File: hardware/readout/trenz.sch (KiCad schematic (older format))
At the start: 1 part, among them J2 Trenz_Module

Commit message: working
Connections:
- net MGT_RX_P3: now reaches J2.A1 (MGT_RX3_P)
- net MGT_TX_N3: now reaches J2.A10 (MGT_TX3_N)
- net MGT_RX_P1: now reaches J2.A13 (MGT_RX1_P)
- net MGT_TX_P2: now reaches J2.A14 (MGT_TX2_P)
- net MGT_RX_N1: now reaches J2.A15 (MGT_RX1_N)
- net MGT_TX_N2: now reaches J2.A16 (MGT_TX2_N)
- net MGT_TX_P1: now reaches J2.A20 (MGT_TX1_P)
- net MGT_TX_N1: now reaches J2.A22 (MGT_TX1_N)
- net MGT_RX_N3: now reaches J2.A3 (MGT_RX3_N)
- net TRIG8: now reaches J2.A49 (B34_L10_P)
- net TRIG9: now reaches J2.A51 (B34_L10_N)
- net TRIG10: now reaches J2.A53 (B34_L11_N)
- net TRIG11: now reaches J2.A55 (B34_L11_P)
- net TRIG12: now reaches J2.A57 (B34_L12_N)
- net TRIG13: now reaches J2.A59 (B34_L12_P)
- net TRIG14: now reaches J2.A63 (B34_L17_N)
- net TRIG15: now reaches J2.A65 (B34_L17_P)
- net TRIG16: now reaches J2.A67 (B34_L21_P)
- net TRIG17: now reaches J2.A69 (B34_L21_N)
- net MGT_RX_P2: now reaches J2.A7 (MGT_RX2_P)
- net TRIG18: now reaches J2.A71 (B34_L19_N)
- net TRIG19: now reaches J2.A73 (B34_L19_P)
- net TRIG20: now reaches J2.A75 (B34_L22_N)
- net TRIG21: now reaches J2.A77 (B34_L22_P)
- net TRIG22: now reaches J2.A79 (B34_L23_N)
- net MGT_TX_P3: now reaches J2.A8 (MGT_TX3_P)
- net TRIG23: now reaches J2.A81 (B34_L23_P)
- net MGT_RX_N2: now reaches J2.A9 (MGT_RX2_N)
- net DATA_RX_N renamed MGT_RX_N0
- net DATA_RX_P renamed MGT_RX_P0
- net DATA_TX_N renamed MGT_TX_N0
- net DATA_TX_P renamed MGT_TX_P0
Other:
- moved on the sheet: J2A, J2B

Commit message: working on schematic
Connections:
- net TRIG0: now also J2.A85 (B14_L24_N); no longer J2.A31 (B34_L2_P)
- net TRIG1: now also J2.A87 (B14_L24_P); no longer J2.A33 (B34_L2_N)
- net TRIG10: now also J2.B63 (B14_L15_P); no longer J2.A53 (B34_L11_N)
- net TRIG11: now also J2.B65 (B14_L15_N); no longer J2.A55 (B34_L11_P)
- net TRIG12: now also J2.B75 (B14_L10_P); no longer J2.A57 (B34_L12_N)
- net TRIG13: now also J2.B77 (B14_L10_N); no longer J2.A59 (B34_L12_P)
- net TRIG14: now also J2.B79 (B14_L16_P); no longer J2.A63 (B34_L17_N)
- net TRIG15: now also J2.B81 (B14_L16_N); no longer J2.A65 (B34_L17_P)
- net TRIG16: now also J2.B85 (B14_L18_N); no longer J2.A67 (B34_L21_P)
- net TRIG17: now also J2.B87 (B14_L18_P); no longer J2.A69 (B34_L21_N)
- net TRIG18: now also J2.B89 (B14_L17_N); no longer J2.A71 (B34_L19_N)
- net TRIG19: now also J2.B91 (B14_L17_P); no longer J2.A73 (B34_L19_P)
- net TRIG2: now also J2.A89 (B14_L23_N); no longer J2.A35 (B34_L1_P)
- net TRIG20: now also J2.B93 (B14_L20_P); no longer J2.A75 (B34_L22_N)
- net TRIG21: now also J2.B95 (B14_L20_N); no longer J2.A77 (B34_L22_P)
- net TRIG22: now also J2.B97 (B14_L25); no longer J2.A79 (B34_L23_N)
- net TRIG23: now also J2.B99 (B14_L0); no longer J2.A81 (B34_L23_P)
- net TRIG3: now also J2.A91 (B14_L23_P); no longer J2.A37 (B34_L1_N)
- net TRIG4: now also J2.A93 (B14_L21_P); no longer J2.A39 (B34_L4_P)
- net TRIG5: now also J2.A95 (B14_L21_N); no longer J2.A41 (B34_L4_N)
- net TRIG6: now also J2.B55 (B14_L4_P); no longer J2.A43 (B34_L5_P)
- net TRIG7: now also J2.B57 (B14_L4_N); no longer J2.A45 (B34_L5_N)
- net TRIG8: now also J2.B59 (B14_L7_N); no longer J2.A49 (B34_L10_P)
- net TRIG9: now also J2.B61 (B14_L7_P); no longer J2.A51 (B34_L10_N)
- net TRIG24: now reaches J2.B56 (B14_L5_P)
- net TRIG25: now reaches J2.B58 (B14_L5_N)
- net TRIG26: now reaches J2.B60 (B14_L8_P)
- net TRIG27: now reaches J2.B62 (B14_L8_N)
- net TRIG28: now reaches J2.B64 (B14_L9_P)
- net TRIG29: now reaches J2.B66 (B14_L9_N)
- net TRIG30: now reaches J2.B74 (B14_L11_N)
- net TRIG31: now reaches J2.B76 (B14_L11_P)
- net TRIG32: now reaches J2.B78 (B14_L14_N)
- net TRIG33: now reaches J2.B80 (B14_L14_P)
- net TRIG34: now reaches J2.B82 (B14_L12_P)
- net TRIG35: now reaches J2.B84 (B14_L12_N)
- net TRIG36: now reaches J2.B86 (B14_L13_N)
- net TRIG37: now reaches J2.B88 (B14_L13_P)
- net TRIG38: now reaches J2.B92 (B14_L19_P)
- net TRIG39: now reaches J2.B94 (B14_L19_N)
- net TRIG40: now reaches J2.B96 (B14_L22_N)
- net TRIG41: now reaches J2.B98 (B14_L22_P)
- net TRIG66: now reaches J2.A32 (B34_L6_P)
- net TRIG67: now reaches J2.A34 (B34_L6_N)
- net TRIG68: now reaches J2.A36 (B34_L7_P)
- net TRIG69: now reaches J2.A38 (B34_L7_N)
- net TRIG70: now reaches J2.A40 (B34_L3_P)
- net TRIG71: now reaches J2.A42 (B34_L3_N)
- net TRIG72: now reaches J2.A44 (B34_L9_P)
- net TRIG73: now reaches J2.A46 (B34_L9_N)
- net TRIG74: now reaches J2.A50 (B34_L8_P)
- net TRIG75: now reaches J2.A52 (B34_L8_N)
- net TRIG76: now reaches J2.A54 (B34_L13_P)
- net TRIG77: now reaches J2.A56 (B34_L13_N)
- net TRIG78: now reaches J2.A58 (B34_L14_P)
- net TRIG79: now reaches J2.A60 (B34_L14_N)
- net TRIG80: now reaches J2.A62 (B34_L15_N)
- net TRIG81: now reaches J2.A64 (B34_L15_P)
- net TRIG82: now reaches J2.A68 (B34_L16_N)
- net TRIG83: now reaches J2.A70 (B34_L16_P)
- net TRIG84: now reaches J2.A72 (B34_L18_P)
- net TRIG85: now reaches J2.A74 (B34_L18_N)
- net TRIG86: now reaches J2.A76 (B34_L20_N)
- net TRIG87: now reaches J2.A78 (B34_L20_P)
- net TRIG88: now reaches J2.A80 (B34_L24_N)
- net TRIG89: now reaches J2.A82 (B34_L24_P)
- new net TRIG42: J2.A31 (B34_L2_P)
- new net TRIG43: J2.A33 (B34_L2_N)
- new net TRIG44: J2.A35 (B34_L1_P)
- new net TRIG45: J2.A37 (B34_L1_N)
- new net TRIG46: J2.A39 (B34_L4_P)
- new net TRIG47: J2.A41 (B34_L4_N)
- new net TRIG48: J2.A43 (B34_L5_P)
- new net TRIG49: J2.A45 (B34_L5_N)
- new net TRIG50: J2.A49 (B34_L10_P)
- new net TRIG51: J2.A51 (B34_L10_N)
- new net TRIG52: J2.A53 (B34_L11_N)
- new net TRIG53: J2.A55 (B34_L11_P)
- new net TRIG54: J2.A57 (B34_L12_N)
- new net TRIG55: J2.A59 (B34_L12_P)
- new net TRIG56: J2.A63 (B34_L17_N)
- new net TRIG57: J2.A65 (B34_L17_P)
- new net TRIG58: J2.A67 (B34_L21_P)
- new net TRIG59: J2.A69 (B34_L21_N)
- new net TRIG60: J2.A71 (B34_L19_N)
- new net TRIG61: J2.A73 (B34_L19_P)
- new net TRIG62: J2.A75 (B34_L22_N)
- new net TRIG63: J2.A77 (B34_L22_P)
- new net TRIG64: J2.A79 (B34_L23_N)
- new net TRIG65: J2.A81 (B34_L23_P)

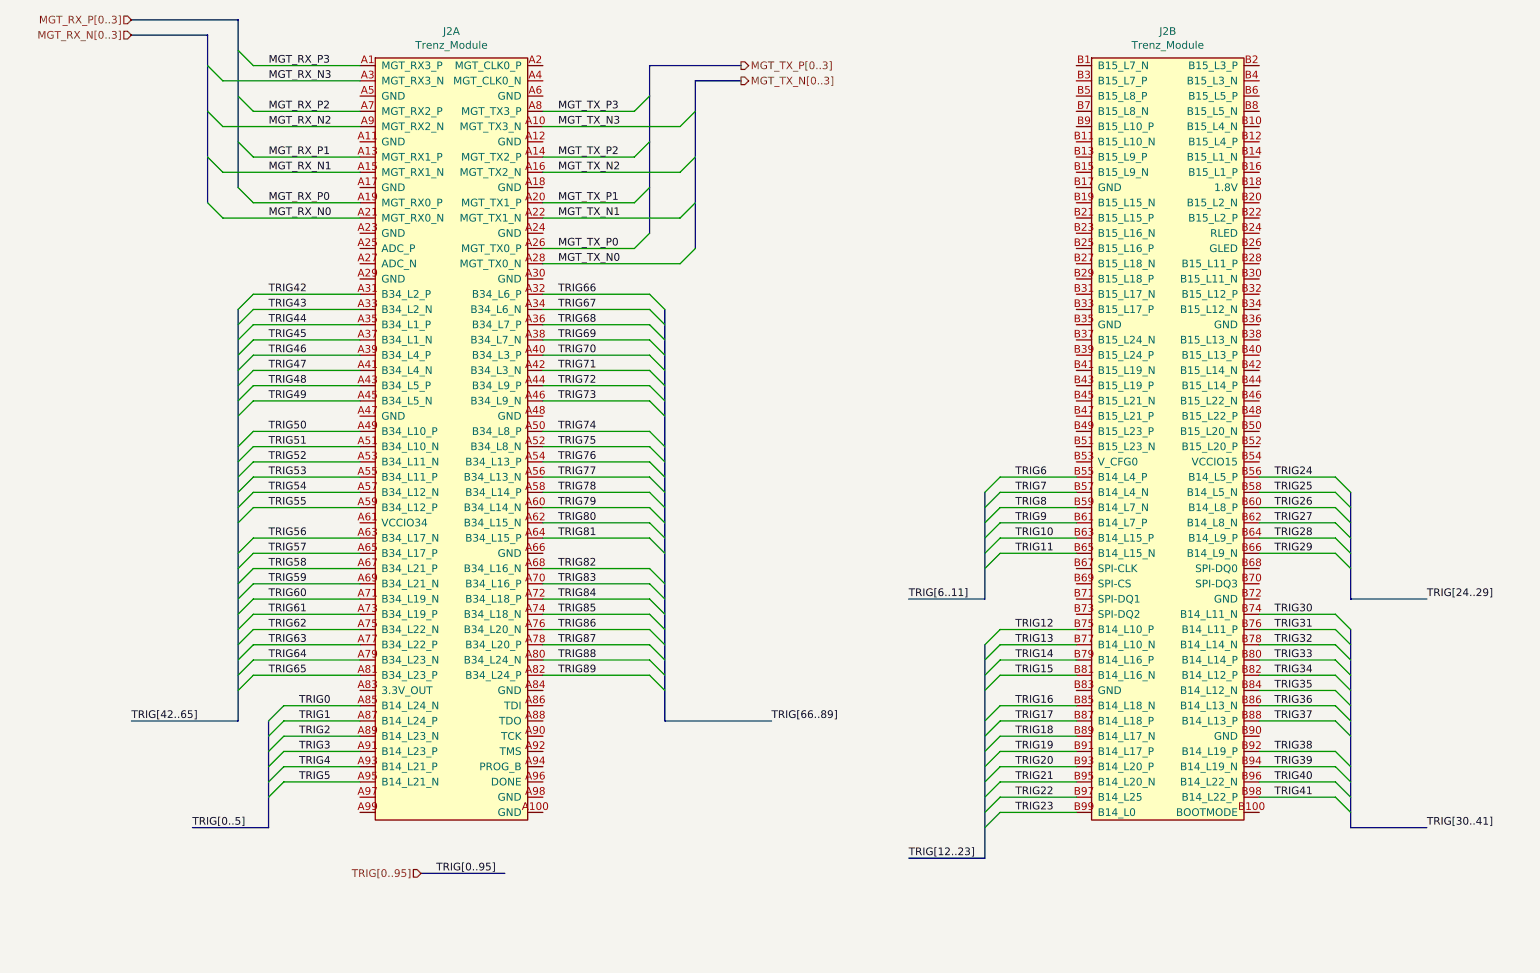
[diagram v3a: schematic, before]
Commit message: Readout schem heirarchy almost done
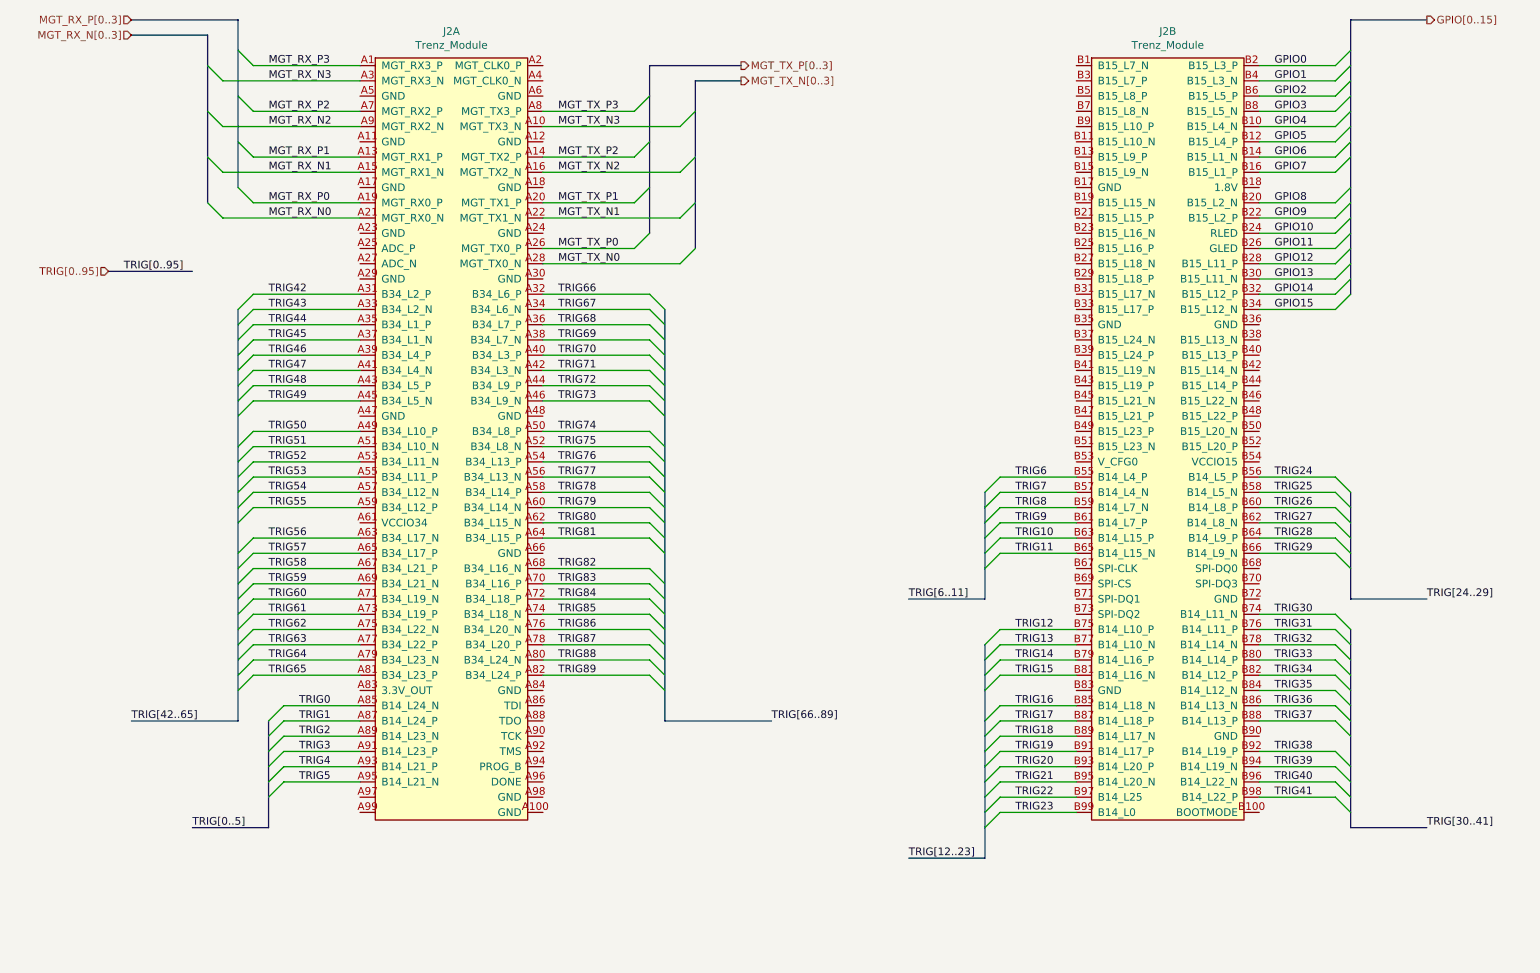
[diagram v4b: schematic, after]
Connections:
- net GPIO4: now reaches J2.B10 (B15_L4_N)
- net GPIO5: now reaches J2.B12 (B15_L4_P)
- net GPIO6: now reaches J2.B14 (B15_L1_N)
- net GPIO7: now reaches J2.B16 (B15_L1_P)
- net GPIO0: now reaches J2.B2 (B15_L3_P)
- net GPIO8: now reaches J2.B20 (B15_L2_N)
- net GPIO9: now reaches J2.B22 (B15_L2_P)
- net GPIO10: now reaches J2.B24 (RLED)
- net GPIO11: now reaches J2.B26 (GLED)
- net GPIO12: now reaches J2.B28 (B15_L11_P)
- net GPIO13: now reaches J2.B30 (B15_L11_N)
- net GPIO14: now reaches J2.B32 (B15_L12_P)
- net GPIO15: now reaches J2.B34 (B15_L12_N)
- net GPIO1: now reaches J2.B4 (B15_L3_N)
- net GPIO2: now reaches J2.B6 (B15_L5_P)
- net GPIO3: now reaches J2.B8 (B15_L5_N)
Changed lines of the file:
@@
 $Descr A4 11693 8268
 encoding utf-8
-Sheet 1 1
+Sheet 9 35
 Title ""
 Date ""
@@
 AR Path="/6109E0BA/61019D1F" Ref="J?"  Part="2"
 AR Path="/6109E0C1/61019D1F" Ref="J?"  Part="2"
+AR Path="/61383376/613835BB/61019D1F" Ref="J?"  Part="2"
+AR Path="/610F1616/613835BB/61019D1F" Ref="J?"  Part="2"
+AR Path="/61119E97/613835BB/61019D1F" Ref="J?"  Part="2"
+AR Path="/61119EA4/613835BB/61019D1F" Ref="J?"  Part="2"
+AR Path="/6111A893/613835BB/61019D1F" Ref="J?"  Part="2"
+AR Path="/6111A8A0/613835BB/61019D1F" Ref="J?"  Part="2"
 F 0 "J?" H 8200 6325 50  0000 C CNN
 F 1 "Trenz_Module" H 8200 6234 50  0000 C CNN
@@
 AR Path="/6109E0BA/6101C3CD" Ref="J?"  Part="1"
 AR Path="/6109E0C1/6101C3CD" Ref="J?"  Part="1"
+AR Path="/61383376/613835BB/6101C3CD" Ref="J?"  Part="1"
+AR Path="/610F1616/613835BB/6101C3CD" Ref="J?"  Part="1"
+AR Path="/61119E97/613835BB/6101C3CD" Ref="J?"  Part="1"
+AR Path="/61119EA4/613835BB/6101C3CD" Ref="J?"  Part="1"
+AR Path="/6111A893/613835BB/6101C3CD" Ref="J?"  Part="1"
+AR Path="/6111A8A0/613835BB/6101C3CD" Ref="J?"  Part="1"
 F 0 "J?" H 3500 6325 50  0000 C CNN
 F 1 "Trenz_Module" H 3500 6234 50  0000 C CNN
@@
 	1    0    0    -1
 $EndComp
-Text HLabel 3300 6500 0    50   Input ~ 0
+Text HLabel 1250 2550 0    50   Input ~ 0
 TRIG[0..95]
 Wire Bus Line
-	3300 6500 3850 6500
-Text Label 3400 6500 0    50   ~ 0
+	1250 2550 1800 2550
+Text Label 1350 2550 0    50   ~ 0
 TRIG[0..95]
 Entry Wire Line
@@
 Text Label 5600 5500 0    50   ~ 0
 TRIG[66..89]
+Entry Wire Line
+	9400 1100 9300 1200
+Entry Wire Line
+	9400 1200 9300 1300
+Entry Wire Line
+	9400 1300 9300 1400
+Entry Wire Line
+	9400 1400 9300 1500
+Entry Wire Line
+	9400 1500 9300 1600
+Entry Wire Line
+	9400 1600 9300 1700
+Entry Wire Line
+	9400 1700 9300 1800
+Entry Wire Line
+	9400 1800 9300 1900
+Entry Wire Line
+	9400 2000 9300 2100
+Entry Wire Line
+	9400 2100 9300 2200
+Entry Wire Line
+	9400 2200 9300 2300
+Entry Wire Line
+	9400 2300 9300 2400
+Entry Wire Line
+	9400 2400 9300 2500
+Entry Wire Line
+	9400 2500 9300 2600
+Entry Wire Line
+	9400 2600 9300 2700
+Entry Wire Line
+	9400 2700 9300 2800
+Wire Wire Line
+	9300 1200 8800 1200
+Wire Wire Line
+	9300 1300 8800 1300
+Wire Wire Line
+	9300 1400 8800 1400
+Wire Wire Line
+	9300 1500 8800 1500
+Wire Wire Line
+	9300 1600 8800 1600
+Wire Wire Line
+	9300 1700 8800 1700
+Wire Wire Line
+	9300 1800 8800 1800
+Wire Wire Line
+	9300 1900 8800 1900
+Wire Wire Line
+	9300 2100 8800 2100
+Wire Wire Line
+	9300 2200 8800 2200
+Wire Wire Line
+	9300 2300 8800 2300
+Wire Wire Line
+	9300 2400 8800 2400
+Wire Wire Line
+	9300 2500 8800 2500
+Wire Wire Line
+	9300 2600 8800 2600
+Wire Wire Line
+	9300 2700 8800 2700
+Wire Wire Line
+	9300 2800 8800 2800
+Text Label 8900 1200 0    50   ~ 0
+GPIO0
+Text Label 8900 1300 0    50   ~ 0
+GPIO1
+Text Label 8900 1400 0    50   ~ 0
+GPIO2
+Text Label 8900 1500 0    50   ~ 0
+GPIO3
+Text Label 8900 1600 0    50   ~ 0
+GPIO4
+Text Label 8900 1700 0    50   ~ 0
+GPIO5
+Text Label 8900 1800 0    50   ~ 0
+GPIO6
+Text Label 8900 1900 0    50   ~ 0
+GPIO7
+Text Label 8900 2100 0    50   ~ 0
+GPIO8
+Text Label 8900 2200 0    50   ~ 0
+GPIO9
+Text Label 8900 2300 0    50   ~ 0
+GPIO10
+Text Label 8900 2400 0    50   ~ 0
+GPIO11
+Text Label 8900 2500 0    50   ~ 0
+GPIO12
+Text Label 8900 2600 0    50   ~ 0
+GPIO13
+Text Label 8900 2700 0    50   ~ 0
+GPIO14
+Text Label 8900 2800 0    50   ~ 0
+GPIO15
+Wire Bus Line
+	9900 900  9400 900
+Text HLabel 9900 900  2    50   Output ~ 0
+GPIO[0..15]
 Wire Bus Line
 	5100 1300 5100 2400
@@
 	9400 4900 9400 6200
 Wire Bus Line
+	9400 900  9400 2700
+Wire Bus Line
 	2100 2800 2100 5500

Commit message: schematic in progress
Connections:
- net CTRL0: now reaches J2.B38 (B15_L13_N)
- net CTRL1: now reaches J2.B40 (B15_L13_P)
- net CTRL2: now reaches J2.B42 (B15_L14_N)
- net CTRL3: now reaches J2.B44 (B15_L14_P)
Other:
- note added: "EMPHATIC readout board\nTrenz TE0714 FPGA module -- 1 of 6"
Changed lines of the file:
@@
 $Descr A4 11693 8268
 encoding utf-8
-Sheet 9 35
+Sheet 12 38
 Title ""
 Date ""
@@
 Text HLabel 9900 900  2    50   Output ~ 0
 GPIO[0..15]
+Entry Wire Line
+	9400 2900 9300 3000
+Entry Wire Line
+	9400 3000 9300 3100
+Entry Wire Line
+	9400 3100 9300 3200
+Entry Wire Line
+	9400 3200 9300 3300
+Wire Wire Line
+	9300 3000 8800 3000
+Wire Wire Line
+	9300 3100 8800 3100
+Wire Wire Line
+	9300 3200 8800 3200
+Wire Wire Line
+	9300 3300 8800 3300
+Text Label 8900 3000 0    50   ~ 0
+CTRL0
+Text Label 8900 3100 0    50   ~ 0
+CTRL1
+Text Label 8900 3200 0    50   ~ 0
+CTRL2
+Text Label 8900 3300 0    50   ~ 0
+CTRL3
+Text HLabel 9950 2800 2    50   Output ~ 0
+CTRL[0..3]
+Wire Bus Line
+	9950 2800 9400 2800
 Wire Bus Line
 	5100 1300 5100 2400
@@
 	2100 900  2100 2000
 Wire Bus Line
+	9400 2800 9400 3200
+Wire Bus Line
 	2300 5500 2300 6200
 Wire Bus Line
@@
 Wire Bus Line
 	4900 2800 4900 5500
+Text Notes 7100 6850 0    75   ~ 0
+EMPHATIC readout board\nTrenz TE0714 FPGA module -- 1 of 6
 $EndSCHEMATC
